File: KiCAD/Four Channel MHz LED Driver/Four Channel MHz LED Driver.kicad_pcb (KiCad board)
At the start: 2 copper layers, 100 x 100 mm, 89 parts, among them J1 Barrel_Jack_Switch, J10 Conn_01x24_Female, J2 Conn_01x02_Female, J3 8P8C_Shielded_x4, J4 Conn_01x03_Male, J5 Conn_01x03_Female, J6 Conn_01x08_Female, J7 Conn_01x03_Female, J8 Conn_01x05_Female, J9 Conn_01x24_Female, M1 Fan_4pin, Q1 SUM70060E, SW1 Pushbutton_with_LED, SW2 Pushbutton_with_LED, SW3 Pushbutton_with_LED, SW4 Pushbutton_with_LED, SW5 SW_SPDT, U1 12V boost, U10 ASSR-1218, U11 ASSR-1218, U12 Teensy3.6, U2 SN74LV4T125PWR, U3 DPBW06F-05, U4 TMUX1204DGSR, U5 HTSOP-J8_ROM, U6 ADP7182AUJZ-1.8-R7, U7 LT6200CS8-10, U8 ASSR-1218, U9 ASSR-1218

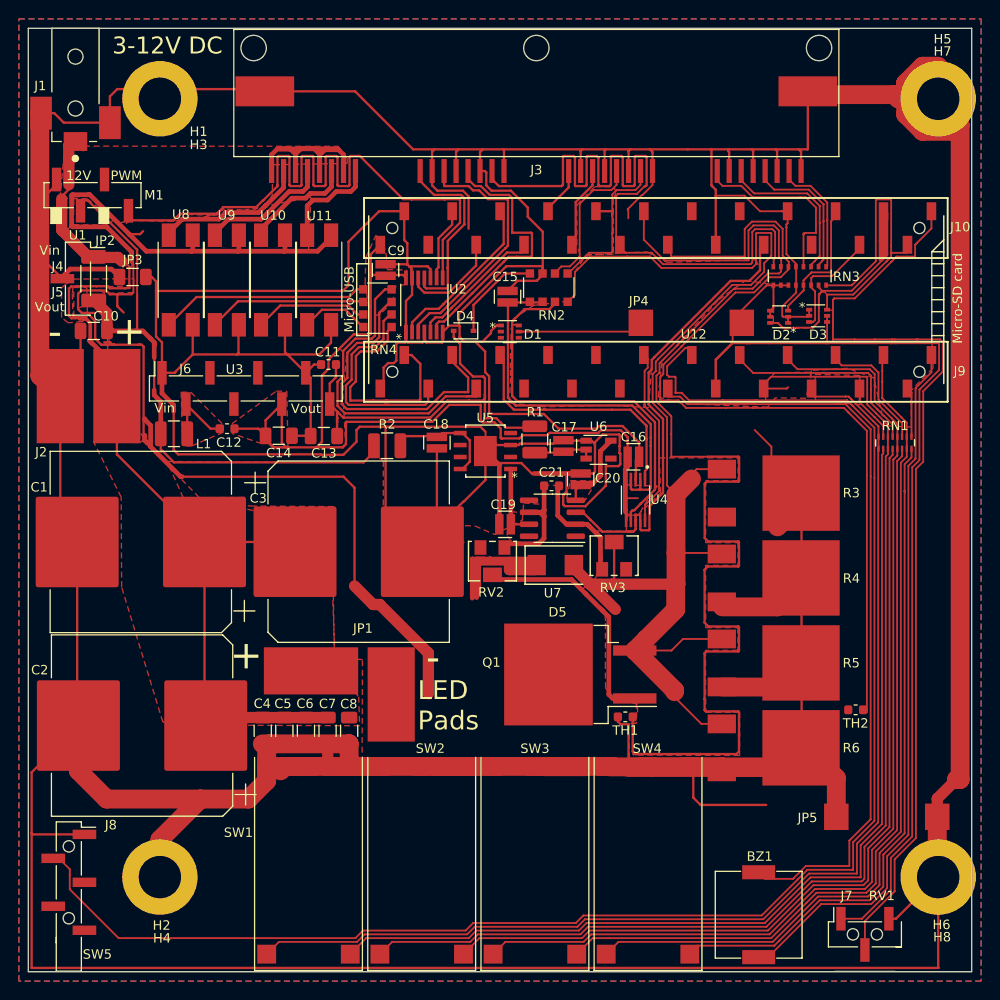
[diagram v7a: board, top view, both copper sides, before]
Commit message: Add logos to schematic and PCB
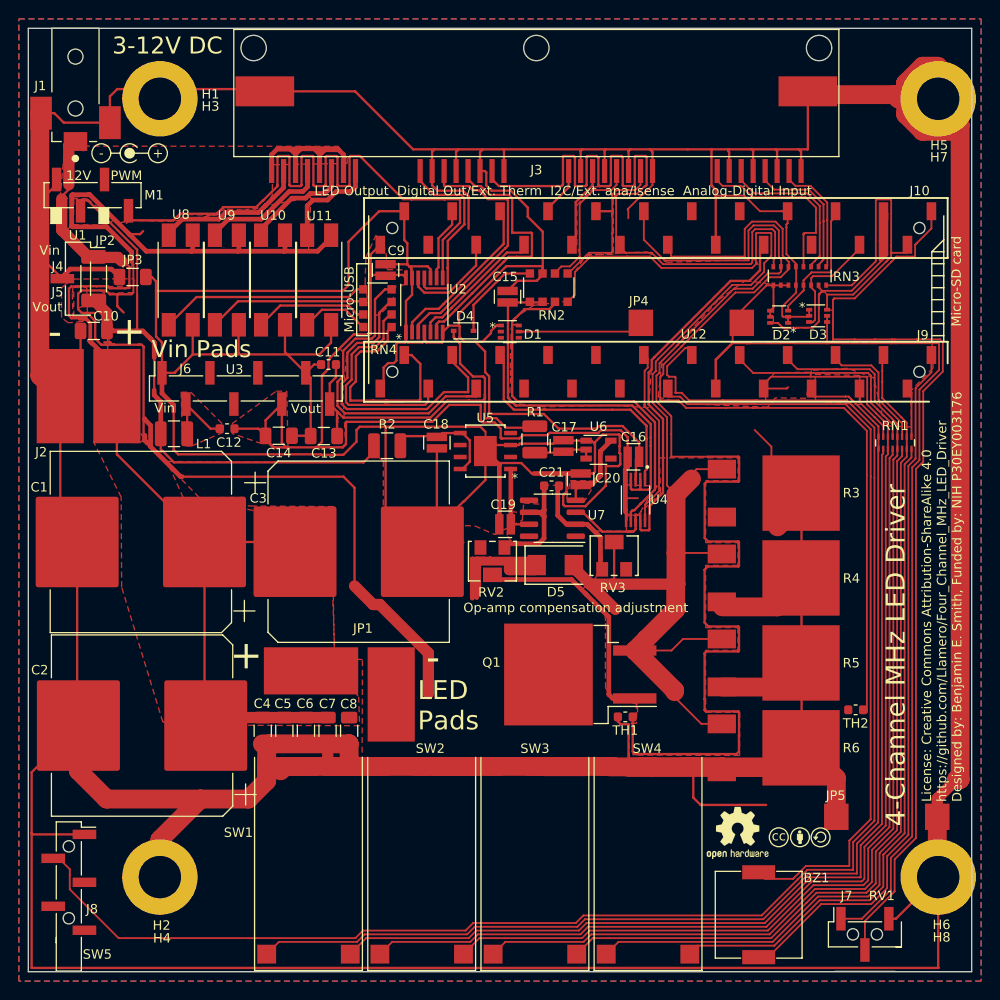
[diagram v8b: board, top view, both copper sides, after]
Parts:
- added LOGO1: CC license, Custom Footprints:Creative_commons_license, F.Cu at (117.5, 108.6)
- added LOGO2: Jack Polarity, Custom Footprints:Polarity_Center_Positive, F.Cu at (47.7, 31.2)
- added LOGO3: OSHW Logo, Symbol:OSHW-Logo2_7.3x6mm_SilkScreen, F.Cu at (112.2, 109.3)
- U5: value HTSOP-J8_ROM -> BDJ0GA5WEFJ-E2
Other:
- board text added: "4-Channel MHz LED Driver"
- board text added: "LED Output Digital Out/Ext. Therm I2C/Ext. ana/Isense Analog-Digital Input"
- board text added: "License: Creative Commons Attribution-ShareAlike 4.0 https://github.com/Llamero/Four_Channel_MHz_LED_Driver Designed by: Benjamin E. Smith, Funded by: NIH P30EY003176"
- board text added: "Op-amp compensation adjustment"
- board text added: "Vin Pads"
